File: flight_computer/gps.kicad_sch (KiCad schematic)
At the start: 7 parts, among them U7 YIC31612EBGG

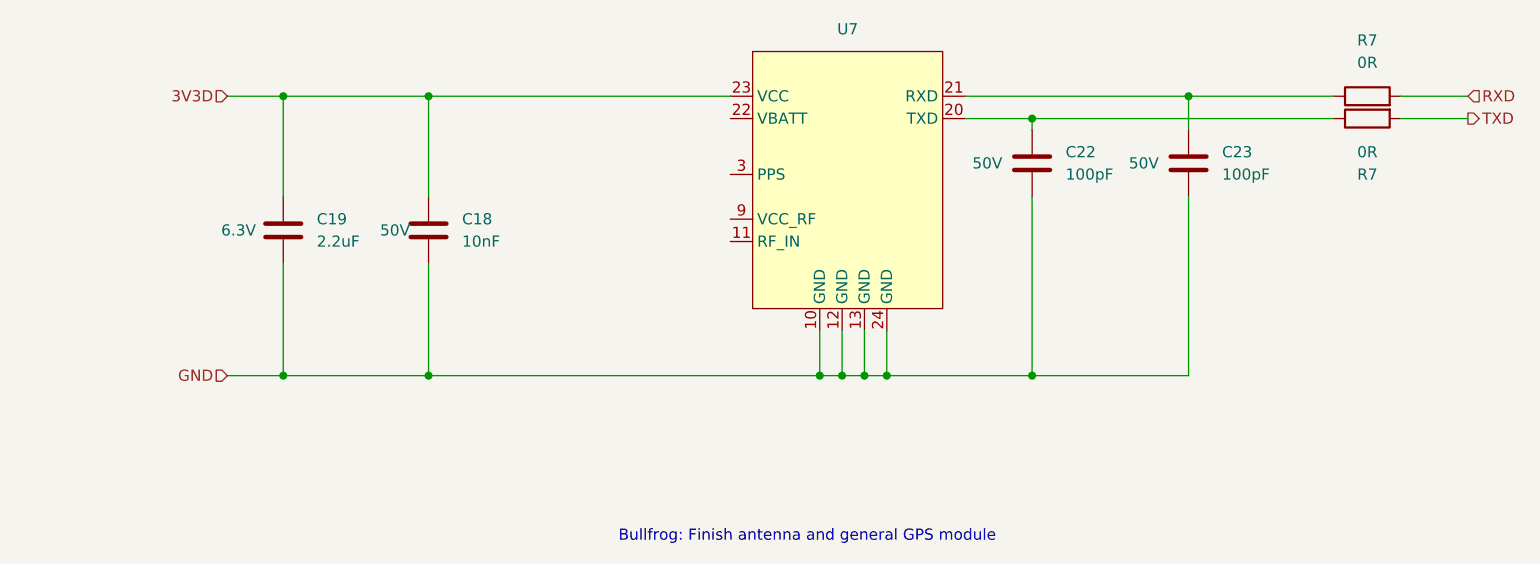
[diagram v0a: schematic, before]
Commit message: Finishing gps, ready to connect all
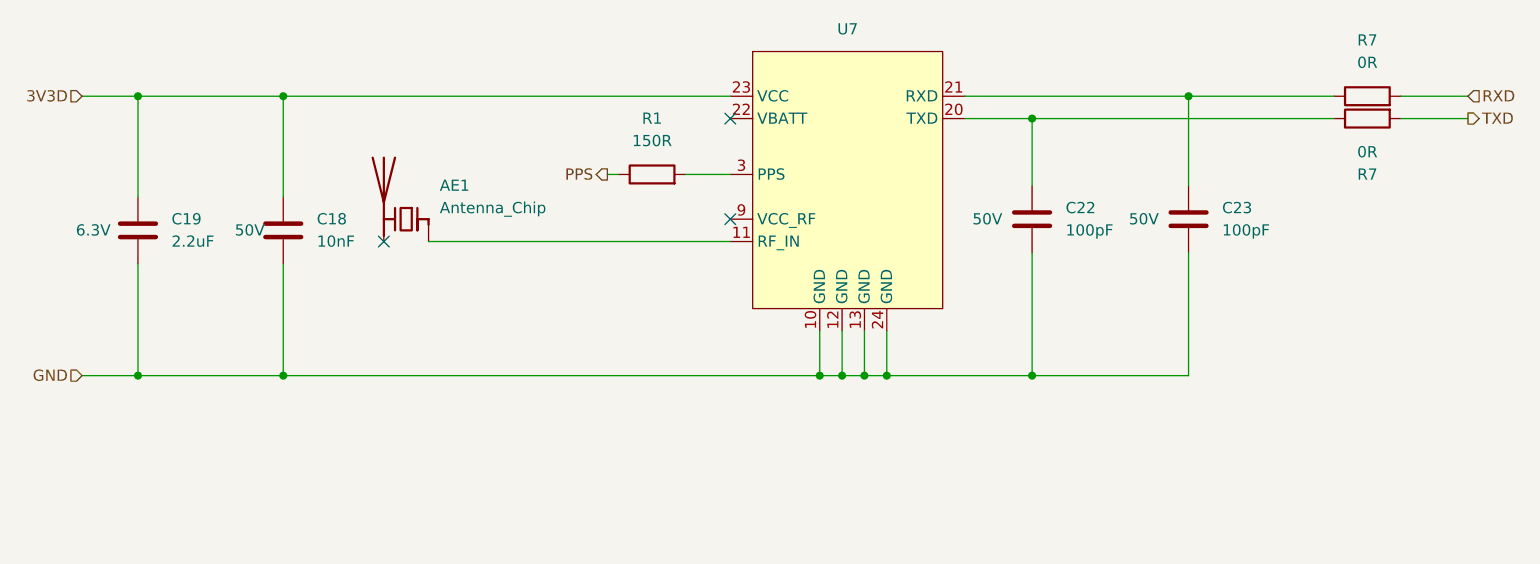
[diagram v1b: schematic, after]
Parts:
- added AE1: Antenna_Chip, my_footprints:ANT_ANT8010LL05R1516A_PUL, symbol Device:Antenna_Chip
- added R1: 150R, Resistor_SMD:R_0402_1005Metric, symbol Device:R
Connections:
- net at U7.11 (RF_IN): now also AE1.1 (FEED)
- net at U7.3 (PPS): now also R1.2
- new net PPS: R1.1
- no-connect marks 0 -> 3
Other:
- note removed: "Bullfrog: Finish antenna and general GPS module"
- moved on the sheet: C18, C19, C22, C23

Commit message: Part way through review
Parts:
- U6: renamed from U7; Manufacturer PN (none) -> YIC31612EBGG; Supplier (none) -> Digikey; Supplier PN (none) -> 3155-YIC31612EBGGCT-ND
- renumbered C22 to C20, C23 to C21
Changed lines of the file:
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@@
   (symbol (lib_id "Device:C") (at 170.18 101.6 0) (unit 1)
     (in_bom yes) (on_board yes) (dnp no)
-    (property "Reference" "C22" (at 173.99 100.33 0)
+    (property "Reference" "C20" (at 173.99 100.33 0)
       (effects (font (size 1.27 1.27)) (justify left))
     )
@@
       (project "flight_computer"
         (path "/89a81c02-14e9-456f-a334-ff69a24bd093/8a1e6a35-f87c-4284-aec3-66a93071d289"
-          (reference "C22") (unit 1)
+          (reference "C20") (unit 1)
         )
       )
@@
   (symbol (lib_id "my_library:YIC31612EBGG") (at 149.86 93.98 0) (unit 1)
     (in_bom yes) (on_board yes) (dnp no) (fields_autoplaced)
-    (property "Reference" "U7" (at 149.225 80.01 0)
+    (property "Reference" "U6" (at 149.225 80.01 0)
       (effects (font (size 1.27 1.27)))
     )
@@
       (effects (font (size 1.27 1.27)) hide)
     )
-    (property "Manufacturer PN" "" (at 149.86 93.98 0)
-      (effects (font (size 1.27 1.27)) hide)
-    )
-    (property "Supplier PN" "" (at 149.86 93.98 0)
-      (effects (font (size 1.27 1.27)) hide)
-    )
-    (property "Supplier" "" (at 149.86 93.98 0)
+    (property "Manufacturer PN" "YIC31612EBGG" (at 149.86 93.98 0)
+      (effects (font (size 1.27 1.27)) hide)
+    )
+    (property "Supplier PN" "3155-YIC31612EBGGCT-ND" (at 149.86 93.98 0)
+      (effects (font (size 1.27 1.27)) hide)
+    )
+    (property "Supplier" "Digikey" (at 149.86 93.98 0)
       (effects (font (size 1.27 1.27)) hide)
     )
@@
       (project "flight_computer"
         (path "/89a81c02-14e9-456f-a334-ff69a24bd093/8a1e6a35-f87c-4284-aec3-66a93071d289"
-          (reference "U7") (unit 1)
+          (reference "U6") (unit 1)
         )
       )
@@
         )
         (path "/89a81c02-14e9-456f-a334-ff69a24bd093/8a1e6a35-f87c-4284-aec3-66a93071d289"
-          (reference "C21") (unit 1)
+          (reference "C18") (unit 1)
         )
       )
@@
         )
         (path "/89a81c02-14e9-456f-a334-ff69a24bd093/8a1e6a35-f87c-4284-aec3-66a93071d289"
-          (reference "C20") (unit 1)
+          (reference "C19") (unit 1)
         )
       )
@@
   (symbol (lib_id "Device:C") (at 187.96 101.6 0) (unit 1)
     (in_bom yes) (on_board yes) (dnp no)
-    (property "Reference" "C23" (at 191.77 100.33 0)
+    (property "Reference" "C21" (at 191.77 100.33 0)
       (effects (font (size 1.27 1.27)) (justify left))
     )
@@
       (project "flight_computer"
         (path "/89a81c02-14e9-456f-a334-ff69a24bd093/8a1e6a35-f87c-4284-aec3-66a93071d289"
-          (reference "C23") (unit 1)
+          (reference "C21") (unit 1)
         )
       )
@@
         )
         (path "/89a81c02-14e9-456f-a334-ff69a24bd093/8a1e6a35-f87c-4284-aec3-66a93071d289"
-          (reference "R21") (unit 1)
-        )
-      )
+          (reference "R18") (unit 1)
+        )
+      )

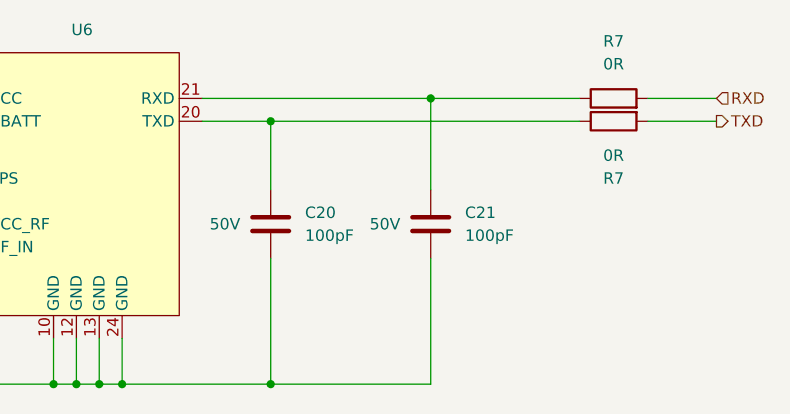
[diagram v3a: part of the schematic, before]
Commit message: Adding shauns thermcoouple
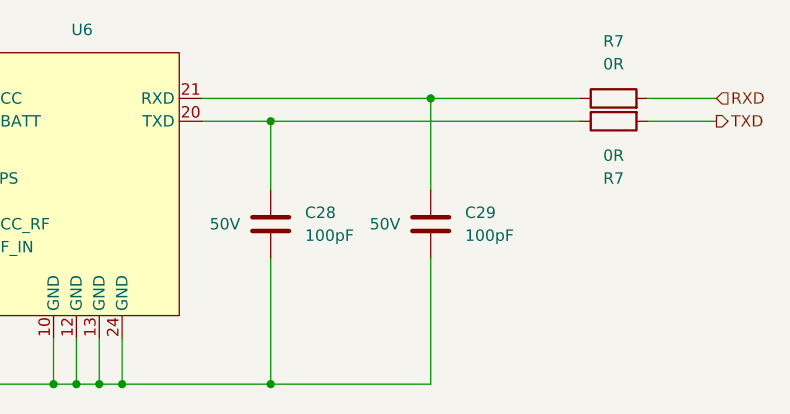
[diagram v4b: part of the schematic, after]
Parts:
- renumbered C20 to C28, C21 to C29
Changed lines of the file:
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@@
   (symbol (lib_id "Device:C") (at 170.18 101.6 0) (unit 1)
     (in_bom yes) (on_board yes) (dnp no)
-    (property "Reference" "C20" (at 173.99 100.33 0)
+    (property "Reference" "C28" (at 173.99 100.33 0)
       (effects (font (size 1.27 1.27)) (justify left))
     )
@@
       (project "flight_computer"
         (path "/89a81c02-14e9-456f-a334-ff69a24bd093/8a1e6a35-f87c-4284-aec3-66a93071d289"
-          (reference "C20") (unit 1)
+          (reference "C28") (unit 1)
         )
       )
@@
         )
         (path "/89a81c02-14e9-456f-a334-ff69a24bd093/8a1e6a35-f87c-4284-aec3-66a93071d289"
-          (reference "C18") (unit 1)
+          (reference "C26") (unit 1)
         )
       )
@@
         )
         (path "/89a81c02-14e9-456f-a334-ff69a24bd093/8a1e6a35-f87c-4284-aec3-66a93071d289"
-          (reference "C19") (unit 1)
+          (reference "C27") (unit 1)
         )
       )
@@
   (symbol (lib_id "Device:C") (at 187.96 101.6 0) (unit 1)
     (in_bom yes) (on_board yes) (dnp no)
-    (property "Reference" "C21" (at 191.77 100.33 0)
+    (property "Reference" "C29" (at 191.77 100.33 0)
       (effects (font (size 1.27 1.27)) (justify left))
     )
@@
       (project "flight_computer"
         (path "/89a81c02-14e9-456f-a334-ff69a24bd093/8a1e6a35-f87c-4284-aec3-66a93071d289"
-          (reference "C21") (unit 1)
-        )
-      )
+          (reference "C29") (unit 1)
+        )
+      )

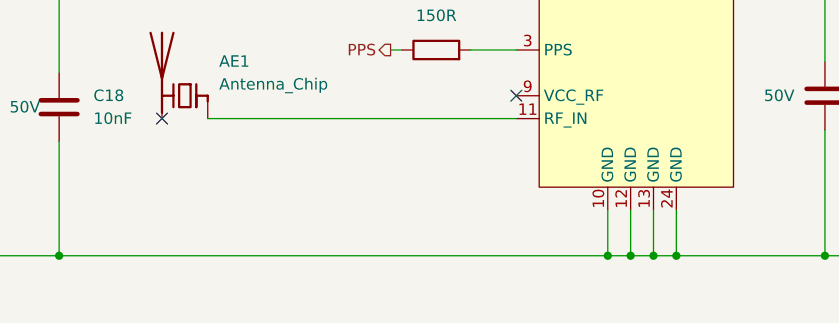
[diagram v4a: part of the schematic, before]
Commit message: GPS antenna controlled impedance
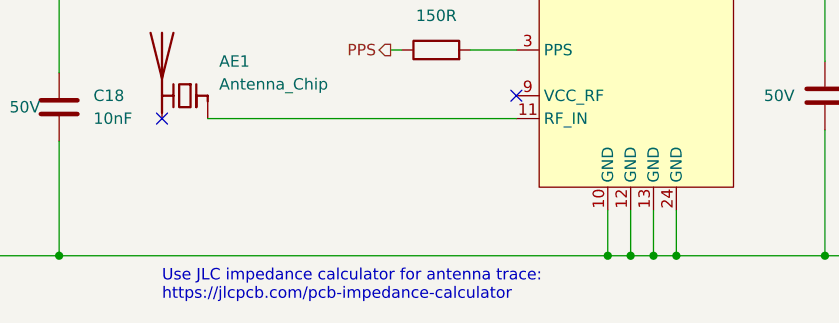
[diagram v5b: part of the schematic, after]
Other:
- note added: "Use JLC impedance calculator for antenna trace: https://jlcpcb.com/pcb-impedance-calculator"
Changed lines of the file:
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@@
     (stroke (width 0) (type default))
+  )
+  (text "Use JLC impedance calculator for antenna trace:\nhttps://jlcpcb.com/pcb-impedance-calculator"
+    (at 96.52 124.46 0)
+    (effects (font (size 1.27 1.27)) (justify left bottom))
   )
   (hierarchical_label "GND" (shape input) (at 62.23 119.38 180) (fields_autoplaced)

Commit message: Most of the way through relayout and new antenna
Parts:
- removed AE1: Antenna_Chip, my_footprints:ANT_ANT8010LL05R1516A_PUL, symbol Device:Antenna_Chip
- added C40, C41: 0.2pF, Capacitor_SMD:C_0402_1005Metric, symbol Device:C
- added L3: 3.9nH, Inductor_SMD:L_0402_1005Metric, symbol Device:L
- added U9: Antenna_GPS, my_footprints:1582AT54A0045, symbol my_library:1582AT54A0045
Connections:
- net GND: now also C40.2, C41.2, U9.2 (GND), U9.4 (GND)
- net at U6.11 (RF_IN): now also C40.1, L3.2
- new net: C41.1, L3.1, U9.1 (Feed)
- no-connect marks 3 -> 2
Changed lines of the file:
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@@
   (junction (at 148.59 119.38) (diameter 0) (color 0 0 0 0)
   )
+  (junction (at 116.84 119.38) (diameter 0) (color 0 0 0 0)
+  )
   (junction (at 151.13 119.38) (diameter 0) (color 0 0 0 0)
   )
@@
   (junction (at 170.18 119.38) (diameter 0) (color 0 0 0 0)
   )
+  (junction (at 128.27 119.38) (diameter 0) (color 0 0 0 0)
+  )
+  (junction (at 128.27 104.14) (diameter 0) (color 0 0 0 0)
+  )
   (junction (at 68.58 87.63) (diameter 0) (color 0 0 0 0)
   )
-  (no_connect (at 96.52 104.14))
+  (junction (at 116.84 104.14) (diameter 0) (color 0 0 0 0)
+  )
+  (junction (at 100.33 119.38) (diameter 0) (color 0 0 0 0)
+  )
+  (junction (at 102.87 119.38) (diameter 0) (color 0 0 0 0)
+  )
   (no_connect (at 135.89 90.17))
   (no_connect (at 135.89 101.6))
@@
     (stroke (width 0) (type default))
   )
+  (wire (pts (xy 128.27 104.14) (xy 135.89 104.14))
+    (stroke (width 0) (type default))
+  )
+  (wire (pts (xy 127 104.14) (xy 128.27 104.14))
+    (stroke (width 0) (type default))
+  )
   (wire (pts (xy 151.13 119.38) (xy 153.67 119.38))
     (stroke (width 0) (type default))
@@
     (stroke (width 0) (type default))
   )
+  (wire (pts (xy 128.27 119.38) (xy 146.05 119.38))
+    (stroke (width 0) (type default))
+  )
   (wire (pts (xy 148.59 119.38) (xy 151.13 119.38))
     (stroke (width 0) (type default))
   )
+  (wire (pts (xy 102.87 119.38) (xy 116.84 119.38))
+    (stroke (width 0) (type default))
+  )
   (wire (pts (xy 62.23 119.38) (xy 68.58 119.38))
     (stroke (width 0) (type default))
@@
     (stroke (width 0) (type default))
   )
+  (wire (pts (xy 110.49 104.14) (xy 116.84 104.14))
+    (stroke (width 0) (type default))
+  )
+  (wire (pts (xy 100.33 119.38) (xy 102.87 119.38))
+    (stroke (width 0) (type default))
+  )
   (wire (pts (xy 68.58 87.63) (xy 85.09 87.63))
     (stroke (width 0) (type default))
@@
     (stroke (width 0) (type default))
   )
+  (wire (pts (xy 100.33 113.03) (xy 100.33 119.38))
+    (stroke (width 0) (type default))
+  )
   (wire (pts (xy 146.05 119.38) (xy 148.59 119.38))
     (stroke (width 0) (type default))
@@
     (stroke (width 0) (type default))
   )
+  (wire (pts (xy 116.84 119.38) (xy 128.27 119.38))
+    (stroke (width 0) (type default))
+  )
   (wire (pts (xy 68.58 106.68) (xy 68.58 119.38))
     (stroke (width 0) (type default))
   )
-  (wire (pts (xy 101.6 104.14) (xy 135.89 104.14))
+  (wire (pts (xy 116.84 104.14) (xy 119.38 104.14))
     (stroke (width 0) (type default))
   )
@@
     (stroke (width 0) (type default))
   )
-  (wire (pts (xy 85.09 119.38) (xy 146.05 119.38))
+  (wire (pts (xy 102.87 113.03) (xy 102.87 119.38))
+    (stroke (width 0) (type default))
+  )
+  (wire (pts (xy 85.09 119.38) (xy 100.33 119.38))
     (stroke (width 0) (type default))
   )
@@
     (stroke (width 0) (type default))
   )
+  (wire (pts (xy 116.84 111.76) (xy 116.84 119.38))
+    (stroke (width 0) (type default))
+  )
   (wire (pts (xy 68.58 99.06) (xy 68.58 87.63))
     (stroke (width 0) (type default))
@@
   )
   (wire (pts (xy 146.05 119.38) (xy 146.05 114.3))
+    (stroke (width 0) (type default))
+  )
+  (wire (pts (xy 128.27 111.76) (xy 128.27 119.38))
     (stroke (width 0) (type default))
   )
@@
   (hierarchical_label "RXD" (shape input) (at 219.71 87.63 0) (fields_autoplaced)
     (effects (font (size 1.27 1.27)) (justify left))
+  )
+  (symbol (lib_id "Device:L") (at 123.19 104.14 90) (unit 1)
+    (in_bom yes) (on_board yes) (dnp no) (fields_autoplaced)
+    (property "Reference" "L3" (at 123.19 99.06 90)
+      (effects (font (size 1.27 1.27)))
+    )
+    (property "Value" "3.9nH" (at 123.19 101.6 90)
+      (effects (font (size 1.27 1.27)))
+    )
+    (property "Footprint" "Inductor_SMD:L_0402_1005Metric" (at 123.19 104.14 0)
+      (effects (font (size 1.27 1.27)) hide)
+    )
+    (property "Datasheet" "https://www.johansontechnology.com/downloads/jti-cat-rf-ind.pdf" (at 123.19 104.14 0)
+      (effects (font (size 1.27 1.27)) hide)
+    )
+    (property "Manufacturer PN" "LRC0402CS3N9GV001T" (at 123.19 104.14 0)
+      (effects (font (size 1.27 1.27)) hide)
+    )
+    (property "Supplier PN" "712-LRC0402CS3N9GV001TCT-ND" (at 123.19 104.14 0)
+      (effects (font (size 1.27 1.27)) hide)
+    )
+    (property "Supplier" "Digikey" (at 123.19 104.14 0)
+      (effects (font (size 1.27 1.27)) hide)
+    )
+    (pin "1")
+    (pin "2")
+    (instances
+      (project "flight_computer"
+        (path "/89a81c02-14e9-456f-a334-ff69a24bd093/8a1e6a35-f87c-4284-aec3-66a93071d289"
+          (reference "L3") (unit 1)
+        )
+      )
+    )
   )
   (symbol (lib_id "Device:C") (at 170.18 101.6 0) (unit 1)
@@
     )
   )
-  (symbol (lib_id "Device:Antenna_Chip") (at 99.06 101.6 0) (mirror y) (unit 1)
-    (in_bom yes) (on_board yes) (dnp no) (fields_autoplaced)
-    (property "Reference" "AE1" (at 102.87 97.79 0)
-      (effects (font (size 1.27 1.27)) (justify right))
-    )
-    (property "Value" "Antenna_Chip" (at 102.87 100.33 0)
-      (effects (font (size 1.27 1.27)) (justify right))
-    )
-    (property "Footprint" "my_footprints:ANT_ANT8010LL05R1516A_PUL" (at 101.6 97.155 0)
-      (effects (font (size 1.27 1.27)) hide)
-    )
-    (property "Datasheet" "https://productfinder.pulseelectronics.com/api/open/part-attachments/datasheet/ANT8010LL05R1516A" (at 101.6 97.155 0)
-      (effects (font (size 1.27 1.27)) hide)
-    )
-    (property "Manufacturer PN" "ANT8010LL05R1516A" (at 99.06 101.6 0)
-      (effects (font (size 1.27 1.27)) hide)
-    )
-    (property "Supplier PN" "311-4601-1-ND" (at 99.06 101.6 0)
-      (effects (font (size 1.27 1.27)) hide)
-    )
-    (property "Supplier" "Digikey" (at 99.06 101.6 0)
-      (effects (font (size 1.27 1.27)) hide)
-    )
-    (pin "1")
-    (pin "2")
-    (instances
-      (project "flight_computer"
-        (path "/89a81c02-14e9-456f-a334-ff69a24bd093/8a1e6a35-f87c-4284-aec3-66a93071d289"
-          (reference "AE1") (unit 1)
+  (symbol (lib_id "Device:C") (at 128.27 107.95 0) (unit 1)
+    (in_bom yes) (on_board yes) (dnp yes) (fields_autoplaced)
+    (property "Reference" "C40" (at 132.08 106.68 0)
+      (effects (font (size 1.27 1.27)) (justify left))
+    )
+    (property "Value" "0.2pF" (at 132.08 109.22 0)
+      (effects (font (size 1.27 1.27)) (justify left))
+    )
+    (property "Footprint" "Capacitor_SMD:C_0402_1005Metric" (at 129.2352 111.76 0)
+      (effects (font (size 1.27 1.27)) hide)
+    )
+    (property "Datasheet" "https://search.murata.co.jp/Ceramy/image/img/A01X/G101/ENG/GJM1555C1HR20BB01-01.pdf" (at 128.27 107.95 0)
+      (effects (font (size 1.27 1.27)) hide)
+    )
+    (property "Manufacturer PN" "GJM1555C1HR20BB01D" (at 128.27 107.95 0)
+      (effects (font (size 1.27 1.27)) hide)
+    )
+    (property "Supplier PN" "490-3078-1-ND" (at 128.27 107.95 0)
+      (effects (font (size 1.27 1.27)) hide)
+    )
+    (property "Supplier" "Digikey" (at 128.27 107.95 0)
+      (effects (font (size 1.27 1.27)) hide)
+    )
+    (pin "1")
+    (pin "2")
+    (instances
+      (project "flight_computer"
+        (path "/89a81c02-14e9-456f-a334-ff69a24bd093/8a1e6a35-f87c-4284-aec3-66a93071d289"
+          (reference "C40") (unit 1)
+        )
+      )
+    )
+  )
+  (symbol (lib_id "Device:C") (at 116.84 107.95 0) (unit 1)
+    (in_bom yes) (on_board yes) (dnp no)
+    (property "Reference" "C41" (at 119.38 106.68 0)
+      (effects (font (size 1.27 1.27)) (justify left))
+    )
+    (property "Value" "0.2pF" (at 119.38 109.22 0)
+      (effects (font (size 1.27 1.27)) (justify left))
+    )
+    (property "Footprint" "Capacitor_SMD:C_0402_1005Metric" (at 117.8052 111.76 0)
+      (effects (font (size 1.27 1.27)) hide)
+    )
+    (property "Datasheet" "https://search.murata.co.jp/Ceramy/image/img/A01X/G101/ENG/GJM1555C1HR20BB01-01.pdf" (at 116.84 107.95 0)
+      (effects (font (size 1.27 1.27)) hide)
+    )
+    (property "Manufacturer PN" "GJM1555C1HR20BB01D" (at 116.84 107.95 0)
+      (effects (font (size 1.27 1.27)) hide)
+    )
+    (property "Supplier PN" "490-3078-1-ND" (at 116.84 107.95 0)
+      (effects (font (size 1.27 1.27)) hide)
+    )
+    (property "Supplier" "Digikey" (at 116.84 107.95 0)
+      (effects (font (size 1.27 1.27)) hide)
+    )
+    (pin "1")
+    (pin "2")
+    (instances
+      (project "flight_computer"
+        (path "/89a81c02-14e9-456f-a334-ff69a24bd093/8a1e6a35-f87c-4284-aec3-66a93071d289"
+          (reference "C41") (unit 1)
         )
       )
@@
         )
       )
+    )
+  )
+  (symbol (lib_id "my_library:1582AT54A0045") (at 102.87 104.14 0) (unit 1)
+    (in_bom yes) (on_board yes) (dnp no)
+    (property "Reference" "U9" (at 99.06 96.52 0)
+      (effects (font (size 1.27 1.27)))
+    )
+    (property "Value" "Antenna_GPS" (at 102.87 99.06 0)
+      (effects (font (size 1.27 1.27)))
+    )
+    (property "Footprint" "my_footprints:1582AT54A0045" (at 105.41 97.79 0)
+      (effects (font (size 1.27 1.27)) hide)
+    )
+    (property "Datasheet" "https://www.johansontechnology.com/datasheets/1582AT54A0045/1582AT54A0045.pdf" (at 106.68 97.79 0)
+      (effects (font (size 1.27 1.27)) hide)
+    )
+    (property "Manufacturer PN" "" (at 102.87 104.14 0)
+      (effects (font (size 1.27 1.27)) hide)
+    )
+    (property "Supplier PN" "" (at 102.87 104.14 0)
+      (effects (font (size 1.27 1.27)) hide)
+    )
+    (property "Supplier" "" (at 102.87 104.14 0)
+      (effects (font (size 1.27 1.27)) hide)
+    )
+    (pin "1")
+    (pin "2")
+    (pin "3")
+    (pin "4")
+    (instances
+      (project "flight_computer"
+        (path "/89a81c02-14e9-456f-a334-ff69a24bd093/8a1e6a35-f87c-4284-aec3-66a93071d289"
+          (reference "U9") (unit 1)
+        )
+      )
